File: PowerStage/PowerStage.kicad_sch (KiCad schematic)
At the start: 19 parts, among them IC1 ATtiny404-SS, IC2 MAX40200AUK, IC3 74LVC1G07GC, IC4 74LVC1G07GC, K1 Conn_01x02, K2 Conn_01x05, K3 DBG/UPDI, Q1 Q_PMOS_GSD

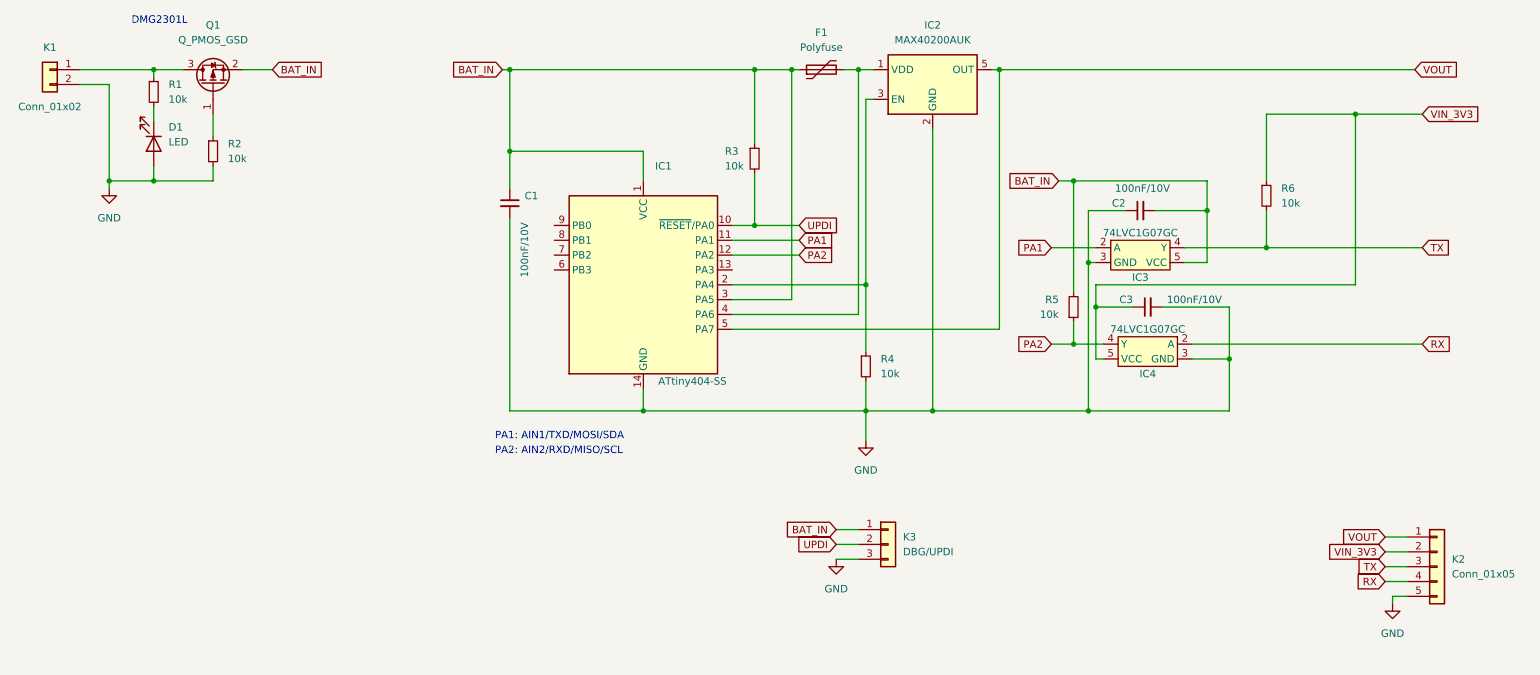
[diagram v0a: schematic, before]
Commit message: Fixes in the schematic
Some fixes in the schematic
Not routed
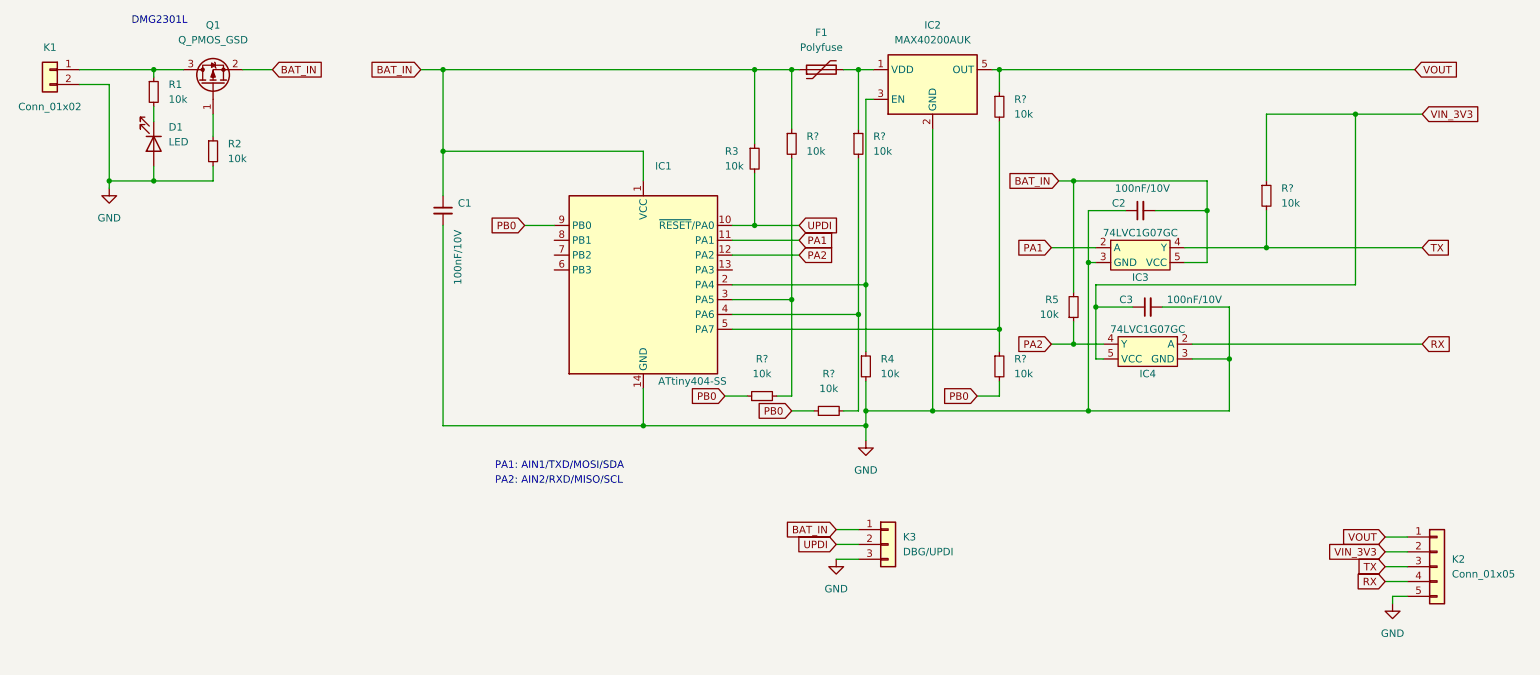
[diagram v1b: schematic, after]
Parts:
- removed R6: 10k, Resistor_SMD:R_0805_2012Metric_Pad1.20x1.40mm_HandSolder, symbol Device:R_Small
- added R? (x7): 10k, Resistor_SMD:R_0805_2012Metric_Pad1.20x1.40mm_HandSolder, symbol Device:R_Small
- IC3, IC4: footprint Package_TO_SOT_SMD:SOT-353_SC-70-5_Handsoldering -> SC-74A_SOT753:SC-74A
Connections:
- net BAT_IN: now also R?.1; no longer IC1.3 (PA5)
- net TX: now also R?.2
- net VIN_3V3: now also R?.1
- net VOUT: now also R?.1; no longer IC1.5 (PA7)
- net at F1.2, IC2.1 (VDD): now also R?.1; no longer IC1.4 (PA6)
- net PB0: now reaches IC1.9 (PB0)
- net PB0: now also R?.1, R?.1, R?.2
- new net: IC1.4 (PA6), R?.2, R?.2
- new net: IC1.3 (PA5), R?.2, R?.2
- new net: IC1.5 (PA7), R?.1, R?.2
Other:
- moved on the sheet: C1

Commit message: Schematics changes
Some modifications in the schematic, need to be routed
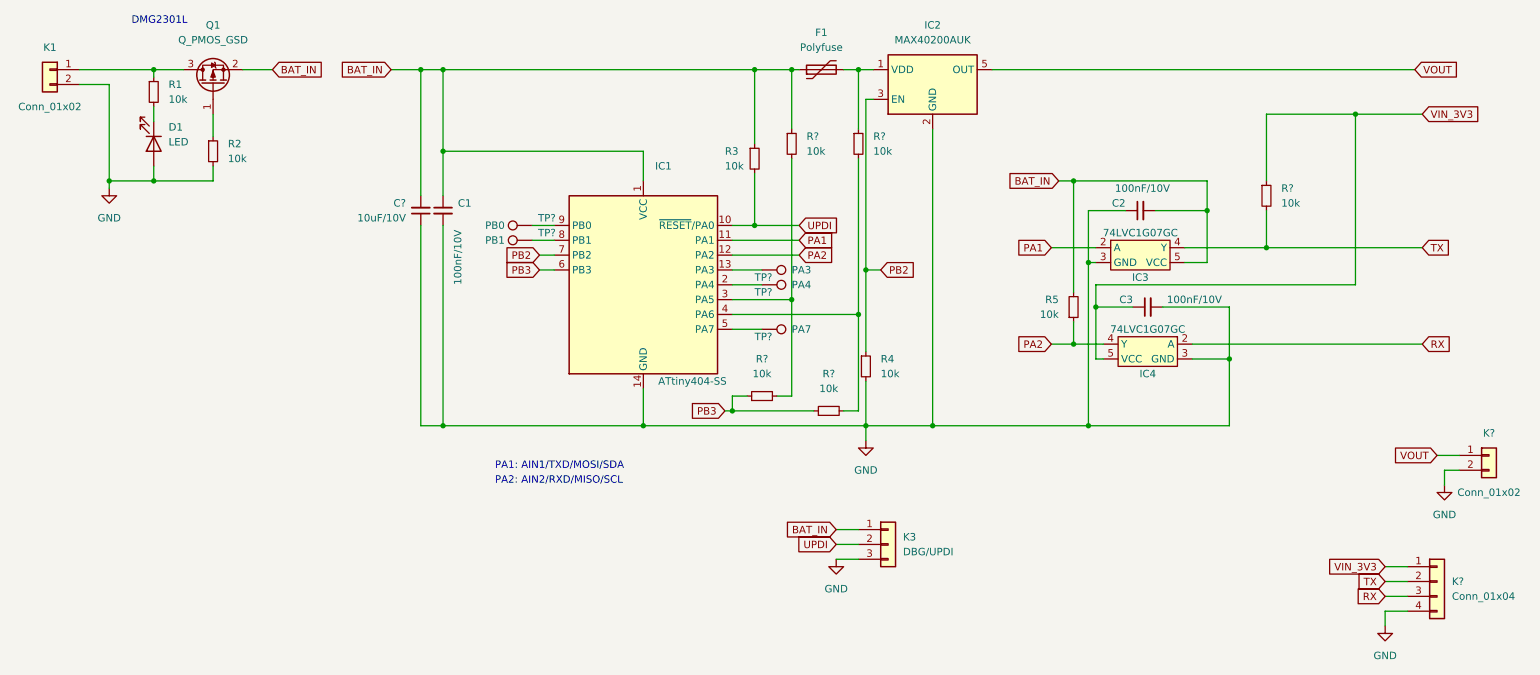
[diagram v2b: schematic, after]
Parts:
- removed K2: Conn_01x05, Connector_PinHeader_2.54mm:PinHeader_1x05_P2.54mm_Vertical, symbol Connector_Generic:Conn_01x05
- removed R? (x2): 10k, Resistor_SMD:R_0805_2012Metric_Pad1.20x1.40mm_HandSolder, symbol Device:R_Small
- added C?: 10uF/10V, symbol Device:C_Small
- added K?: Conn_01x02, Connector_PinHeader_2.54mm:PinHeader_1x02_P2.54mm_Vertical, symbol Connector_Generic:Conn_01x02
- added K?: Conn_01x04, symbol Connector_Generic:Conn_01x04
- added TP?: PA4, symbol Connector:TestPoint
- added TP?: PA7, symbol Connector:TestPoint
- added TP?: PB1, symbol Connector:TestPoint
- added TP?: PA3, symbol Connector:TestPoint
- added TP?: PB0, symbol Connector:TestPoint
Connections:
- net BAT_IN: now also C?.2
- net GND: now also C?.1, K?.2 (Pin_2), K?.4 (Pin_4)
- net RX: now also K?.3 (Pin_3)
- net TX: now also K?.2 (Pin_2)
- net VIN_3V3: now also K?.1 (Pin_1)
- net VOUT: now also K?.1 (Pin_1)
- net at IC1.5 (PA7): now also TP?.1
- net at IC1.13 (PA3): now also TP?.1
- net PB2: now reaches IC2.3 (EN), R4.1
- net PB2: now also IC1.7 (PB2); no longer IC1.2 (PA4)
- net PB3: now reaches IC1.6 (PB3)
- net PB3: now also R?.1, R?.1
- net at IC1.8 (PB1): now also TP?.1
- removed net PB0: IC1.9 (PB0), R?.1, R?.1
- new net: IC1.2 (PA4), TP?.1
- new net: IC1.9 (PB0), TP?.1

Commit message: Updated PCB
PCB and Schamtic has been updated
Not neeed connections removed
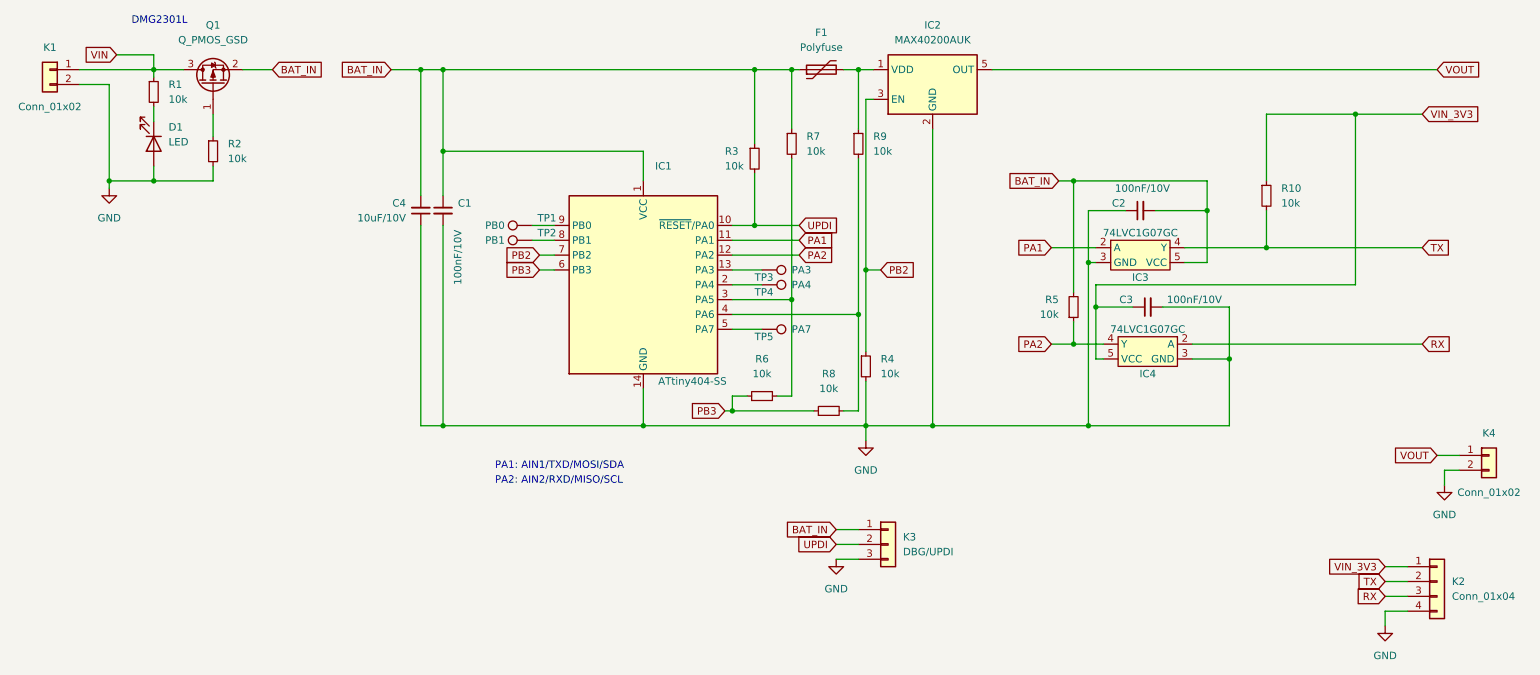
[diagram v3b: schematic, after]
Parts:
- C4: renamed from C?; footprint (none) -> Capacitor_SMD:C_0805_2012Metric_Pad1.18x1.45mm_HandSolder
- K2: renamed from K?; footprint (none) -> Connector_PinSocket_2.54mm:PinSocket_1x04_P2.54mm_Vertical
- TP1, TP2, TP3, TP4, TP5: renamed from TP?; footprint (none) -> TestPoint:TestPoint_Pad_D1.0mm
- gave numbers to parts that had none: 6
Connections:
- net VIN: now reaches K1.1 (Pin_1), Q1.3 (D), R1.1

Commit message: Files for Rev 2 order
Designe send to Aisler
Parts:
- renumbered TP3 to PA3, TP4 to PA4, TP5 to PA7, TP1 to PB0, TP2 to PB1
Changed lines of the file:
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@@
   (symbol (lib_id "Connector:TestPoint") (at 152.4 62.23 270) (unit 1)
     (in_bom yes) (on_board yes)
-    (property "Reference" "TP4" (id 0) (at 151.13 63.5 90)
+    (property "Reference" "PA4" (id 0) (at 151.13 63.5 90)
       (effects (font (size 1.27 1.27)) (justify left))
     )
@@
   (symbol (lib_id "Connector:TestPoint") (at 152.4 69.85 270) (unit 1)
     (in_bom yes) (on_board yes)
-    (property "Reference" "TP5" (id 0) (at 151.13 71.12 90)
+    (property "Reference" "PA7" (id 0) (at 151.13 71.12 90)
       (effects (font (size 1.27 1.27)) (justify left))
     )
@@
   (symbol (lib_id "Connector:TestPoint") (at 113.03 54.61 90) (unit 1)
     (in_bom yes) (on_board yes)
-    (property "Reference" "TP2" (id 0) (at 115.57 53.34 90))
+    (property "Reference" "PB1" (id 0) (at 115.57 53.34 90))
     (property "Value" "PB1" (id 1) (at 106.68 54.61 90))
     (property "Footprint" "TestPoint:TestPoint_Pad_D1.0mm" (id 2) (at 113.03 49.53 0)
@@
   (symbol (lib_id "Connector:TestPoint") (at 152.4 59.69 270) (unit 1)
     (in_bom yes) (on_board yes)
-    (property "Reference" "TP3" (id 0) (at 151.13 60.96 90)
+    (property "Reference" "PA3" (id 0) (at 151.13 60.96 90)
       (effects (font (size 1.27 1.27)) (justify left))
     )
@@
   (symbol (lib_id "Connector:TestPoint") (at 113.03 52.07 90) (unit 1)
     (in_bom yes) (on_board yes)
-    (property "Reference" "TP1" (id 0) (at 115.57 50.8 90))
+    (property "Reference" "PB0" (id 0) (at 115.57 50.8 90))
     (property "Value" "PB0" (id 1) (at 106.68 52.07 90))
     (property "Footprint" "TestPoint:TestPoint_Pad_D1.0mm" (id 2) (at 113.03 46.99 0)
@@
       (reference "K4") (unit 1) (value "Conn_01x02") (footprint "Connector_PinHeader_2.54mm:PinHeader_1x02_P2.54mm_Vertical")
     )
+    (path "/d7f44e46-534a-4682-b620-a566a94ae2f2"
+      (reference "PA3") (unit 1) (value "PA3") (footprint "TestPoint:TestPoint_Pad_D1.0mm")
+    )
+    (path "/28e107ee-143f-40c0-b046-11adab8f9079"
+      (reference "PA4") (unit 1) (value "PA4") (footprint "TestPoint:TestPoint_Pad_D1.0mm")
+    )
+    (path "/4ec69c2d-93b8-4d4a-866e-f1862390fc5c"
+      (reference "PA7") (unit 1) (value "PA7") (footprint "TestPoint:TestPoint_Pad_D1.0mm")
+    )
+    (path "/e9d55dfa-b32b-49a7-a5a4-10feb68007c5"
+      (reference "PB0") (unit 1) (value "PB0") (footprint "TestPoint:TestPoint_Pad_D1.0mm")
+    )
+    (path "/6eb58fd5-4c1b-4b1f-8d9d-621e1cf03e8d"
+      (reference "PB1") (unit 1) (value "PB1") (footprint "TestPoint:TestPoint_Pad_D1.0mm")
+    )
     (path "/e621dda4-652f-463a-980f-9351f5fcbc20"
       (reference "Q1") (unit 1) (value "Q_PMOS_GSD") (footprint "Package_TO_SOT_SMD:SOT-23")
@@
       (reference "R10") (unit 1) (value "10k") (footprint "Resistor_SMD:R_0805_2012Metric_Pad1.20x1.40mm_HandSolder")
     )
-    (path "/e9d55dfa-b32b-49a7-a5a4-10feb68007c5"
-      (reference "TP1") (unit 1) (value "PB0") (footprint "TestPoint:TestPoint_Pad_D1.0mm")
-    )
-    (path "/6eb58fd5-4c1b-4b1f-8d9d-621e1cf03e8d"
-      (reference "TP2") (unit 1) (value "PB1") (footprint "TestPoint:TestPoint_Pad_D1.0mm")
-    )
-    (path "/d7f44e46-534a-4682-b620-a566a94ae2f2"
-      (reference "TP3") (unit 1) (value "PA3") (footprint "TestPoint:TestPoint_Pad_D1.0mm")
-    )
-    (path "/28e107ee-143f-40c0-b046-11adab8f9079"
-      (reference "TP4") (unit 1) (value "PA4") (footprint "TestPoint:TestPoint_Pad_D1.0mm")
-    )
-    (path "/4ec69c2d-93b8-4d4a-866e-f1862390fc5c"
-      (reference "TP5") (unit 1) (value "PA7") (footprint "TestPoint:TestPoint_Pad_D1.0mm")
-    )
-  )
+  )
